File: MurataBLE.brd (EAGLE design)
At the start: 90 x 70 mm, 54 parts, among them CON1 47589-0001, IC1 I-5448, IC2 LPC11U35_QFN33, IC3 NC7SZ00, IC4 AT25DN512C, IC5 AT25XE011, P1 NC, P2 NC, P3 NC, P4 NC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

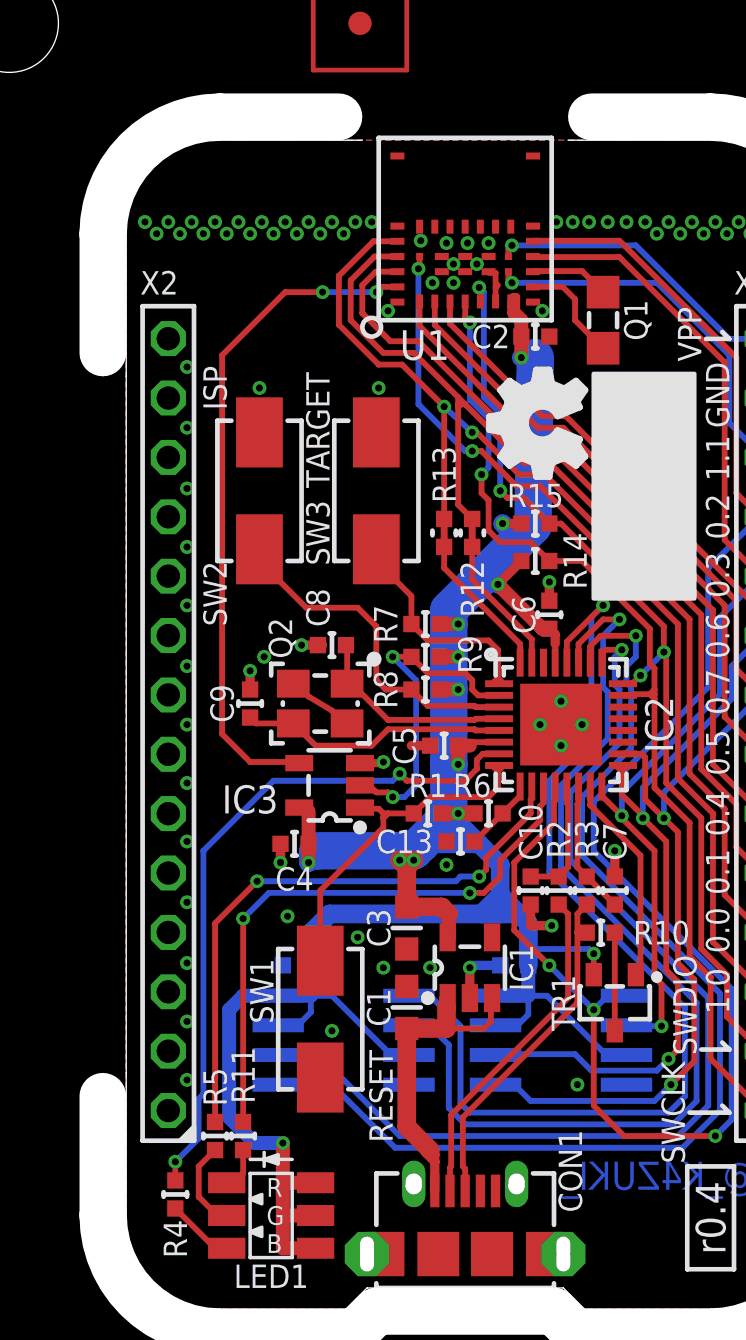
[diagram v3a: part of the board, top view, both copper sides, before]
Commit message: [ USB ] add LED2, R16-18
UART TX/RX LEDs and blinky a LED combined to LED2
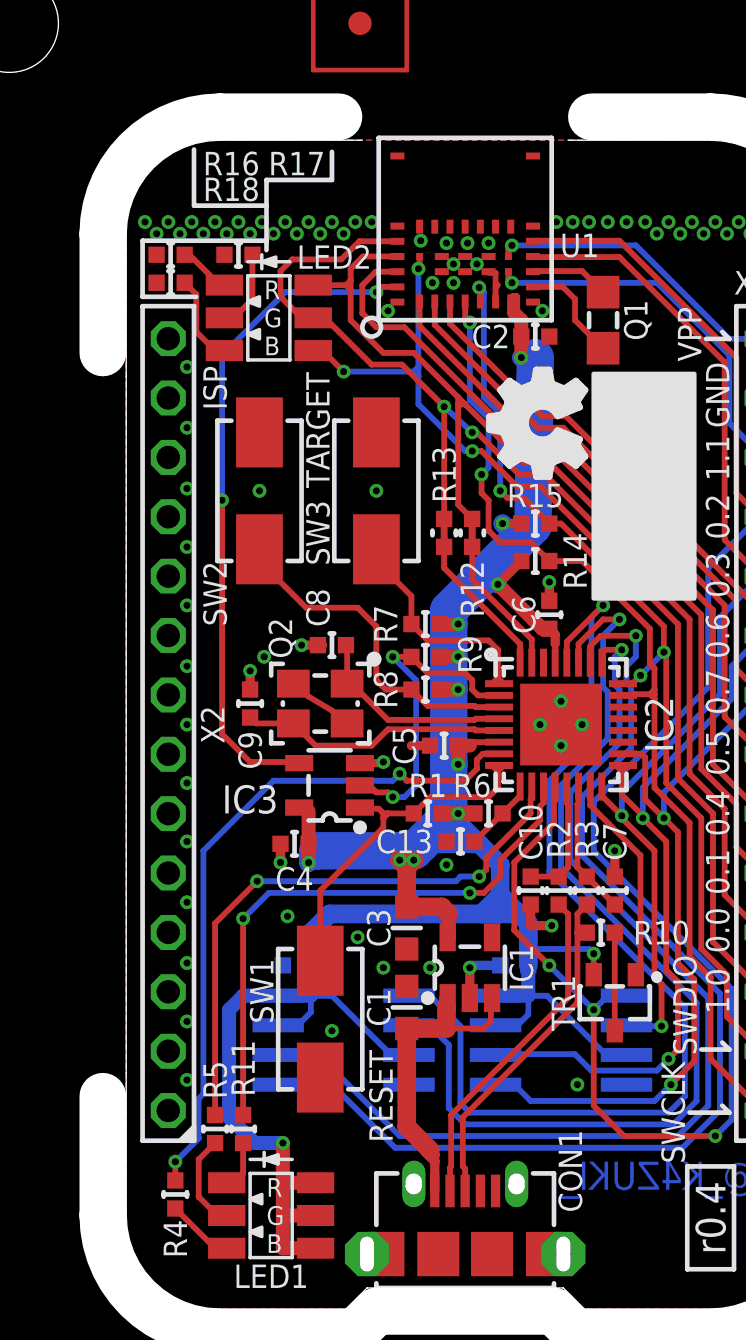
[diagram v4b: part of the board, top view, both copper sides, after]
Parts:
- added LED2: LED_3SEG, mylib:LED_3SEG_SMD
- added R16, R17, R18: 1k/1005, mylib:C0402
- moved R11 0.30 mm to (15.0, 17.7)
- moved R5 0.30 mm to (13.8, 17.7)
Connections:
- new net N$14: LED2.3, R18.1
- new net N$15: LED2.2, R17.1
- new net N$16: LED2.1, R16.1
- net 580.P0_0: now also LED2.4
- net 580.P0_1: now also LED2.5
- net 580.P1_0: now also LED2.6
- net GND: now also R16.2, R17.2, R18.2
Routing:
- net 580.P1_0: track 38.6 -> 43.8 mm, vias 2 -> 3
- net 580.P0_1: track 44.9 -> 49.3 mm
- net N$14: track 0.00 -> 3.84 mm
- net N$15: track 0.00 -> 3.43 mm
- net 580.P0_0: track 42.4 -> 44.6 mm
- net N$16: track 0.00 -> 2.24 mm

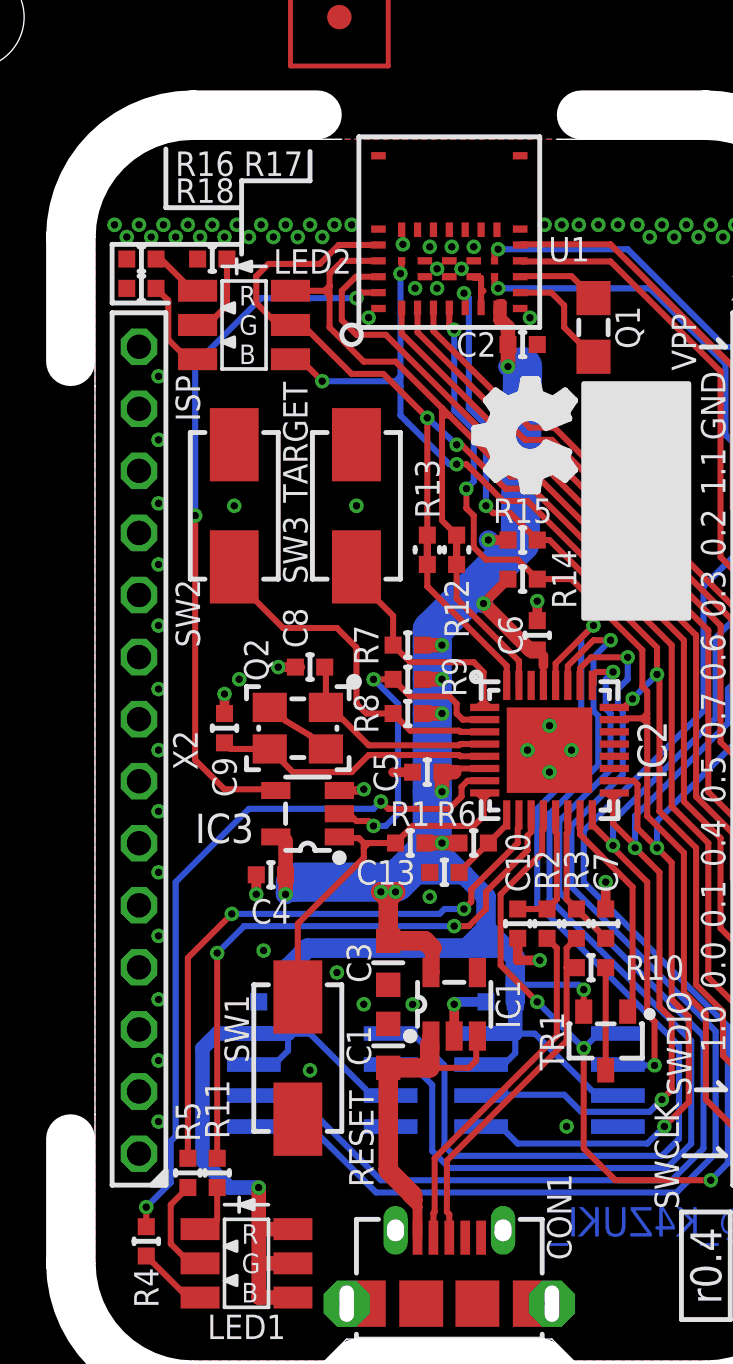
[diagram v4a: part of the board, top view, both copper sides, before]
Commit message: [ USB ] IC1 replace and necessary moves
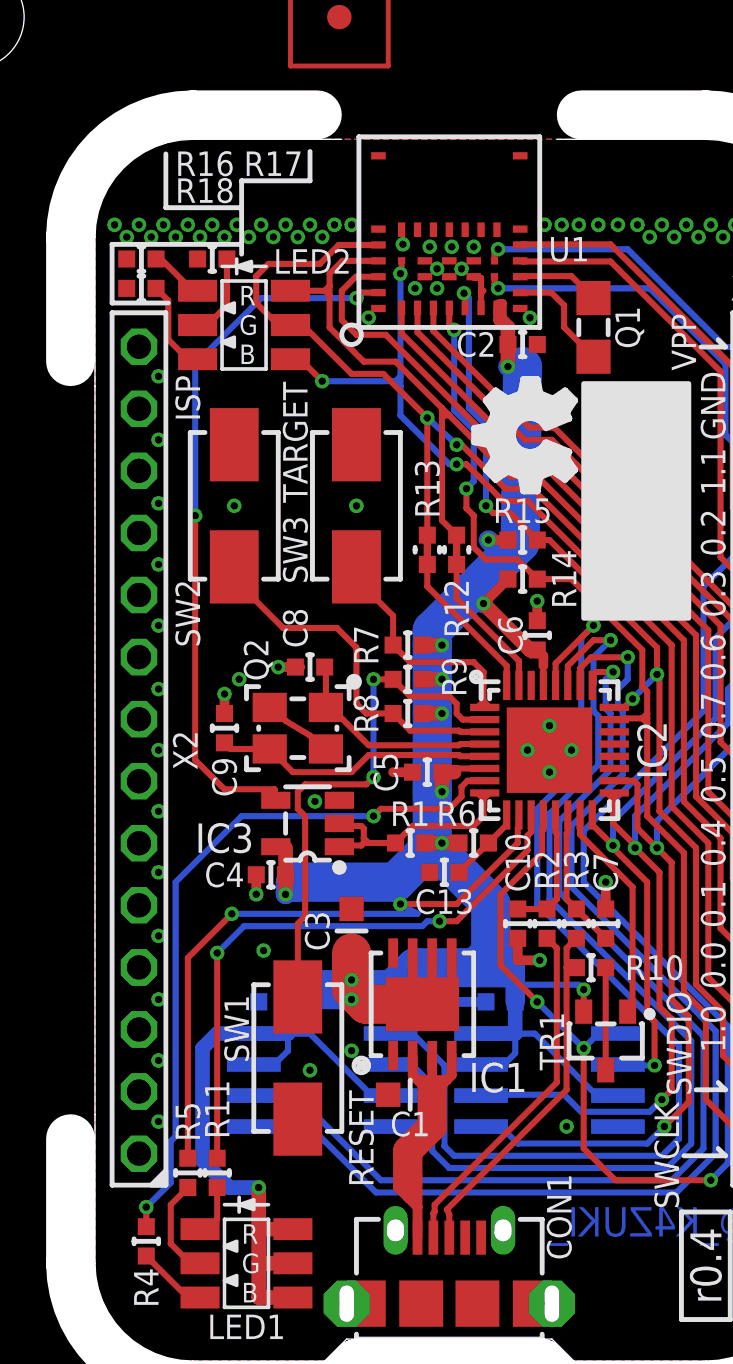
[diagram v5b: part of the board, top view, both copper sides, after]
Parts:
- IC1: value I-5448 -> (none); device mylib:SOT95P280X145-5N -> mylib:DFN80P410X410_8N
- moved C1 2.19 mm to (22.9, 20.9), turned to 180 degrees
- moved C3 1.98 mm to (20.5, 27.6), turned to 90 degrees
- moved IC1 1.30 mm to (23.4, 24.6), turned to 0 degrees
- moved IC3 0.40 mm to (18.7, 32.0)
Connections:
- removed net N$5: IC2.2, IC3.2, R9.2
- new net NSRST: IC2.8, IC3.1, IC3.2, R1.2
- net !RESET!: now also IC2.2, R9.2; no longer IC2.8, IC3.1, R1.2
- net 3.3V: now also IC1.6, IC1.7, IC1.EP
- net GND: now also IC1.1; no longer IC1.2
- net VUSB: now also IC1.2, IC1.4; no longer IC1.1
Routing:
- net N$5: track 14.2 -> 0.00 mm, vias 2 -> 0
- net NSRST: track 0.00 -> 10.0 mm
- net !RESET!: track 15.7 -> 21.5 mm, vias 0 -> 2
- net 3.3V: track 126.3 -> 130.7 mm
- net GND: track 17.2 -> 13.9 mm, vias 83 -> 79
- net VUSB: track 14.5 -> 16.8 mm
- net N$9: track 25.1 -> 26.2 mm

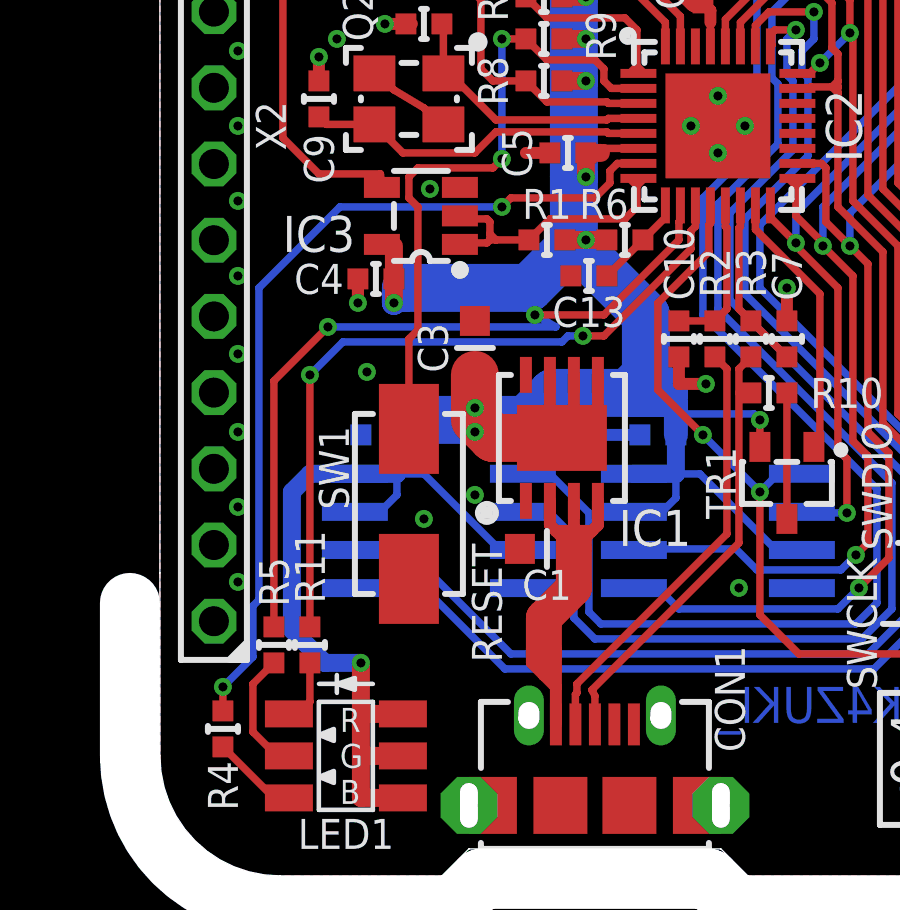
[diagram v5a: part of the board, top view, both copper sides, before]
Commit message: [ USB ] fix DRC error
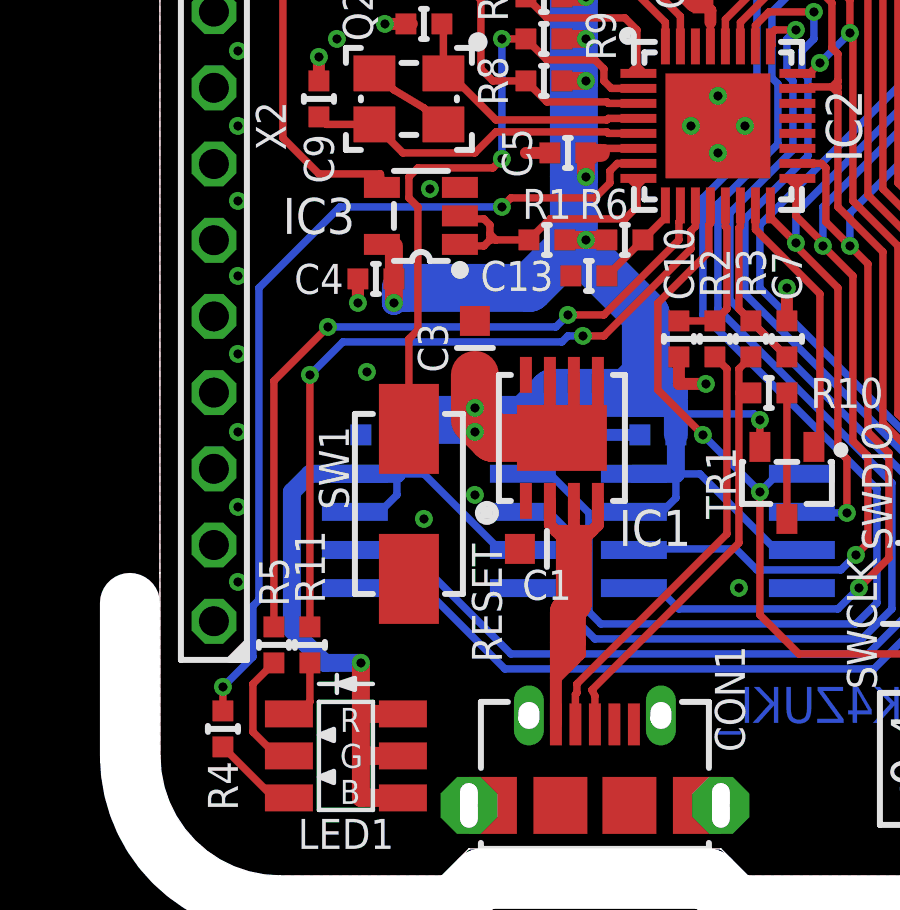
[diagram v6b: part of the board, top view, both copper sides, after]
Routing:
- net N$9: track 26.2 -> 24.8 mm
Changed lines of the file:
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@@
 <text x="26.3" y="25.9" size="1" layer="126" ratio="20" rot="SMR0" align="center">C11</text>
 <text x="17.3" y="25.9" size="1" layer="126" ratio="20" rot="SMR0" align="center">C12</text>
-<text x="24.3" y="28.8" size="1" layer="125" ratio="20" align="center">C13</text>
+<text x="21.9" y="30" size="1" layer="125" ratio="20" align="center">C13</text>
 <text x="29" y="15.9" size="1" layer="125" ratio="20" rot="R90" align="center">CON1</text>
 <text x="26.5" y="21.6" size="1.2" layer="125" ratio="17" align="center">IC1</text>
 <text x="32.8" y="35" size="1.2" layer="125" ratio="17" rot="R90" align="center">IC2</text>
-<text x="15.29999375" y="31.4000125" size="1.2" layer="125" ratio="17" rot="SR0" align="center">IC3</text>
+<text x="15.29999375" y="32.0000125" size="1.2" layer="125" ratio="17" rot="SR0" align="center">IC3</text>
 <text x="19.3" y="18.2" size="1.2" layer="126" ratio="17" rot="SMR0" align="center">IC4</text>
 <text x="28.6" y="18.2" size="1.2" layer="126" ratio="17" rot="MR180" align="center">IC5</text>
@@
 <attribute name="MOUSER" value="" x="24.3" y="30" size="1.778" layer="27" rot="R180" display="off"/>
 <attribute name="AKIZUKI" value="" x="24.3" y="30" size="1.778" layer="27" rot="R180" display="off"/>
-<attribute name="NAME" x="24.3" y="28.8" size="1" layer="25" font="vector" ratio="20" align="center"/>
+<attribute name="NAME" x="21.9" y="30" size="1" layer="25" font="vector" ratio="20" align="center"/>
 <attribute name="VALUE" x="24.3" y="30" size="1" layer="27" font="vector" rot="R180" align="center"/>
 </element>
@@
 <element name="IC3" library="mylib" package="SOT95P280X145-5N" value="NC7SZ00" x="18.7" y="32" smashed="yes" rot="R180">
 <attribute name="DIGIKEY" value="NC7SZ00M5XCT-ND" x="18.7" y="32" size="1.778" layer="27" rot="R180" display="off"/>
-<attribute name="NAME" x="15.3" y="31.4" size="1.2" layer="25" font="vector" ratio="17" rot="SR0" align="center"/>
+<attribute name="NAME" x="15.3" y="32" size="1.2" layer="25" font="vector" ratio="17" rot="SR0" align="center"/>
 <attribute name="VALUE" x="18.7" y="32" size="1.2" layer="27" rot="SR180" align="center"/>
 </element>
@@
 <contactref element="C1" pad="1"/>
 <contactref element="CON1" pad="1"/>
-<wire x1="23.2" y1="15.05" x2="23.2" y2="16.3" width="0.4" layer="1"/>
-<wire x1="23.2" y1="16.3" x2="23.2" y2="16.9" width="0.4" layer="1"/>
-<wire x1="23.2" y1="16.9" x2="22.8" y2="17.3" width="0.4" layer="1"/>
-<wire x1="23.2" y1="16.9" x2="23.2" y2="17.6" width="0.4" layer="1"/>
-<wire x1="22.8" y1="16.7" x2="23.2" y2="16.3" width="0.4" layer="1"/>
+<wire x1="23.2" y1="15.05" x2="23.2" y2="16.6" width="0.4" layer="1"/>
 <contactref element="IC1" pad="4"/>
 <contactref element="IC1" pad="3"/>
@@
 <wire x1="23.2" y1="21.5" x2="23.8" y2="21.5" width="0.4" layer="1"/>
 <wire x1="23.8" y1="21.5" x2="24.4" y2="21.5" width="0.4" layer="1"/>
-<wire x1="23.8" y1="20.9" x2="23.8" y2="19.6" width="1.2" layer="1"/>
-<wire x1="23.8" y1="19.6" x2="22.8" y2="18.6" width="1.2" layer="1"/>
-<wire x1="22.8" y1="18.6" x2="22.8" y2="17.3" width="1.2" layer="1"/>
-<wire x1="22.8" y1="16.7" x2="22.4" y2="17.1" width="0.4" layer="1"/>
-<wire x1="22.4" y1="17.1" x2="22.4" y2="17.6" width="0.4" layer="1"/>
-<wire x1="22.8" y1="16.7" x2="22.8" y2="17.3" width="0.4" layer="1"/>
+<wire x1="23.8" y1="20.9" x2="23.8" y2="19.1" width="1.2" layer="1"/>
+<wire x1="23.8" y1="19.1" x2="23.6" y2="18.8" width="1.2" layer="1"/>
+<wire x1="23.6" y1="18.8" x2="23.6" y2="17.8" width="1.2" layer="1"/>
+<wire x1="23.2" y1="16.6" x2="23.6" y2="17" width="0.4" layer="1"/>
+<wire x1="23.6" y1="17" x2="23.8" y2="17.2" width="0.4" layer="1"/>
+<wire x1="23.8" y1="17.2" x2="24" y2="17.4" width="0.4" layer="1"/>
 <wire x1="23.4" y1="21.3" x2="23.4" y2="20.9" width="0.4" layer="1"/>
 <wire x1="24.2" y1="21.3" x2="24.2" y2="20.9" width="0.4" layer="1"/>
+<wire x1="24" y1="17.4" x2="24" y2="17.8" width="0.4" layer="1"/>
+<wire x1="23.6" y1="17.8" x2="24" y2="17.8" width="0.4" layer="1"/>
+<wire x1="23.6" y1="17.8" x2="23.6" y2="17" width="0.4" layer="1"/>
+<wire x1="23.2" y1="16.6" x2="23.2" y2="17.2" width="0.4" layer="1"/>
+<wire x1="23.2" y1="17.2" x2="23.2" y2="17.8" width="0.4" layer="1"/>
+<wire x1="23.2" y1="17.2" x2="23.8" y2="17.2" width="0.4" layer="1"/>
 </signal>
 <signal name="N$20">
@@
 <contactref element="IC3" pad="2"/>
 <wire x1="20" y1="32" x2="20" y2="31.9" width="0.25" layer="1"/>
-<wire x1="20" y1="31.05" x2="20" y2="31.1" width="0.25" layer="1"/>
-<wire x1="20" y1="31.1" x2="20.9" y2="31.1" width="0.25" layer="1"/>
-<wire x1="20.9" y1="31.1" x2="21" y2="31.2" width="0.25" layer="1"/>
-<wire x1="20" y1="31.9" x2="20.9" y2="31.9" width="0.25" layer="1"/>
-<wire x1="20.9" y1="31.9" x2="21" y2="31.8" width="0.25" layer="1"/>
-<wire x1="21" y1="31.8" x2="21" y2="31.4" width="0.25" layer="1"/>
+<wire x1="20" y1="31.05" x2="20" y2="31" width="0.25" layer="1"/>
+<wire x1="20" y1="31" x2="20.8" y2="31" width="0.25" layer="1"/>
+<wire x1="20.8" y1="31" x2="21" y2="31.2" width="0.25" layer="1"/>
+<wire x1="20" y1="31.9" x2="20.8" y2="31.9" width="0.25" layer="1"/>
+<wire x1="20.8" y1="31.9" x2="21" y2="31.7" width="0.25" layer="1"/>
+<wire x1="21" y1="31.7" x2="21" y2="31.4" width="0.25" layer="1"/>
 <wire x1="21" y1="31.4" x2="21" y2="31.2" width="0.25" layer="1"/>
 <wire x1="21" y1="31.2" x2="21.2" y2="31.2" width="0.25" layer="1"/>
@@
 <contactref element="R5" pad="1"/>
 <contactref element="IC2" pad="10"/>
-<via x="22.5" y="28.7" extent="1-16" drill="0.3"/>
+<via x="23.6" y="28.7" extent="1-16" drill="0.3"/>
 <wire x1="15.6" y1="28.3" x2="23.2" y2="28.3" width="0.25" layer="16"/>
-<wire x1="23.2" y1="28.3" x2="22.5" y2="28.7" width="0.25" layer="16"/>
+<wire x1="23.2" y1="28.3" x2="23.6" y2="28.7" width="0.25" layer="16"/>
 <wire x1="27.35" y1="32.35" x2="27.35" y2="31.85" width="0.25" layer="1"/>
 <wire x1="27.35" y1="31.85" x2="27.3" y2="31.8" width="0.25" layer="1"/>
-<wire x1="22.5" y1="28.7" x2="24.8" y2="28.7" width="0.25" layer="1"/>
+<wire x1="23.6" y1="28.7" x2="24.8" y2="28.7" width="0.25" layer="1"/>
 <wire x1="24.8" y1="28.7" x2="27.3" y2="31.2" width="0.25" layer="1"/>
 <wire x1="27.3" y1="31.2" x2="27.3" y2="31.8" width="0.25" layer="1"/>

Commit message: [ USB ] trace
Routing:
- net GND: vias 79 -> 80
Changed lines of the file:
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@@
 <contactref element="R18" pad="2"/>
 <contactref element="IC1" pad="1"/>
+<via x="25.8" y="16.3" extent="1-16" drill="0.3" diameter="0.45"/>
 </signal>
 <signal name="N$2">
@@
 <contactref element="CON1" pad="3"/>
 <wire x1="29.3" y1="26.1" x2="29.3" y2="21.1" width="0.25" layer="1"/>
-<wire x1="24.5" y1="15.05" x2="24.5" y2="16" width="0.25" layer="1"/>
-<wire x1="24.5" y1="16" x2="24.4" y2="16.2" width="0.25" layer="1"/>
+<wire x1="24.5" y1="15.05" x2="24.5" y2="15.5" width="0.25" layer="1"/>
+<wire x1="24.5" y1="15.5" x2="24.4" y2="15.6" width="0.25" layer="1"/>
+<wire x1="24.4" y1="15.6" x2="24.4" y2="16.2" width="0.25" layer="1"/>
 <wire x1="24.4" y1="16.2" x2="29.3" y2="21.1" width="0.25" layer="1"/>
 <wire x1="29.7" y1="26.1" x2="29.3" y2="26.1" width="0.25" layer="1"/>
@@
 <wire x1="28.9" y1="26.9" x2="28.9" y2="21.4" width="0.25" layer="1"/>
 <contactref element="CON1" pad="2"/>
-<wire x1="23.9" y1="16.4" x2="23.9" y2="16.1" width="0.25" layer="1"/>
-<wire x1="23.85" y1="15.05" x2="23.85" y2="16.05" width="0.25" layer="1"/>
-<wire x1="23.85" y1="16.05" x2="23.9" y2="16.1" width="0.25" layer="1"/>
+<wire x1="23.9" y1="16.4" x2="23.9" y2="15.6" width="0.25" layer="1"/>
+<wire x1="23.85" y1="15.05" x2="23.85" y2="15.55" width="0.25" layer="1"/>
+<wire x1="23.85" y1="15.55" x2="23.9" y2="15.6" width="0.25" layer="1"/>
 <wire x1="28.9" y1="26.9" x2="28.5" y2="27.3" width="0.25" layer="1"/>
 <wire x1="23.9" y1="16.4" x2="28.9" y2="21.4" width="0.25" layer="1"/>
